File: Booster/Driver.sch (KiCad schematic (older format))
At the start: 4 parts

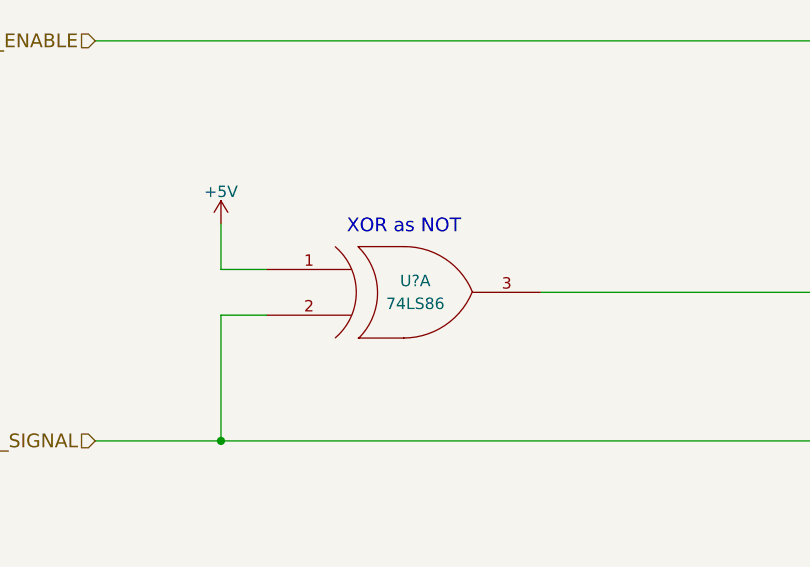
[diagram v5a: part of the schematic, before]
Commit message: Use actual test point instead of 1 pin jumpers.
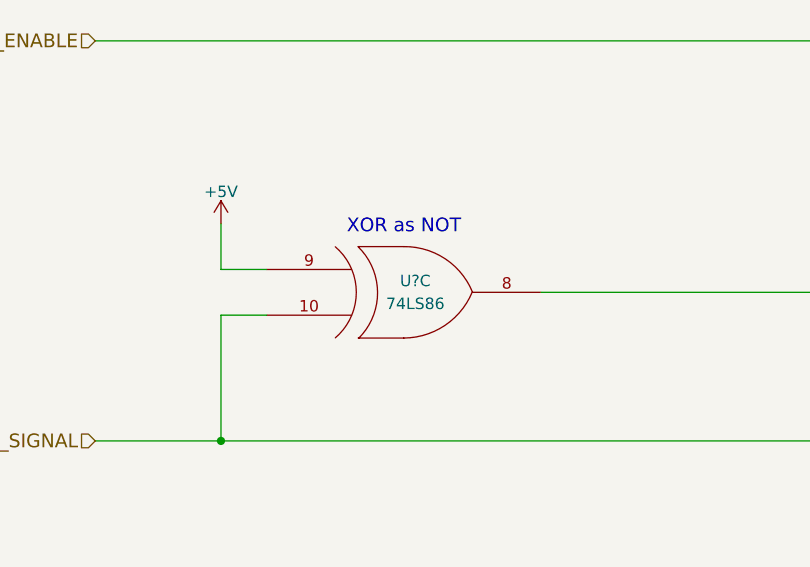
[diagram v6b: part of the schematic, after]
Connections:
- net +5V: now also U?.9 (IN1); no longer U?.1 (IN1)
- net DRIVER_SIGNAL: now also U?.10 (IN2); no longer U?.2 (IN2)
- net at IC?.15 (SIG2A), IC?.2 (SIG1A): now also U?.8 (OUT); no longer U?.3 (OUT)
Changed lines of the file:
@@
 $Comp
 L 74LS86 U?
-U 1 1 5A0F63C2
+U 3 1 5A0F63C2
 P 3800 4850
 F 0 "U?" H 3850 4900 50  0000 C CNN
@@
 F 2 "" H 3800 4850 50  0001 C CNN
 F 3 "" H 3800 4850 50  0001 C CNN
-	1    3800 4850
+	3    3800 4850
 	1    0    0    -1
 $EndComp

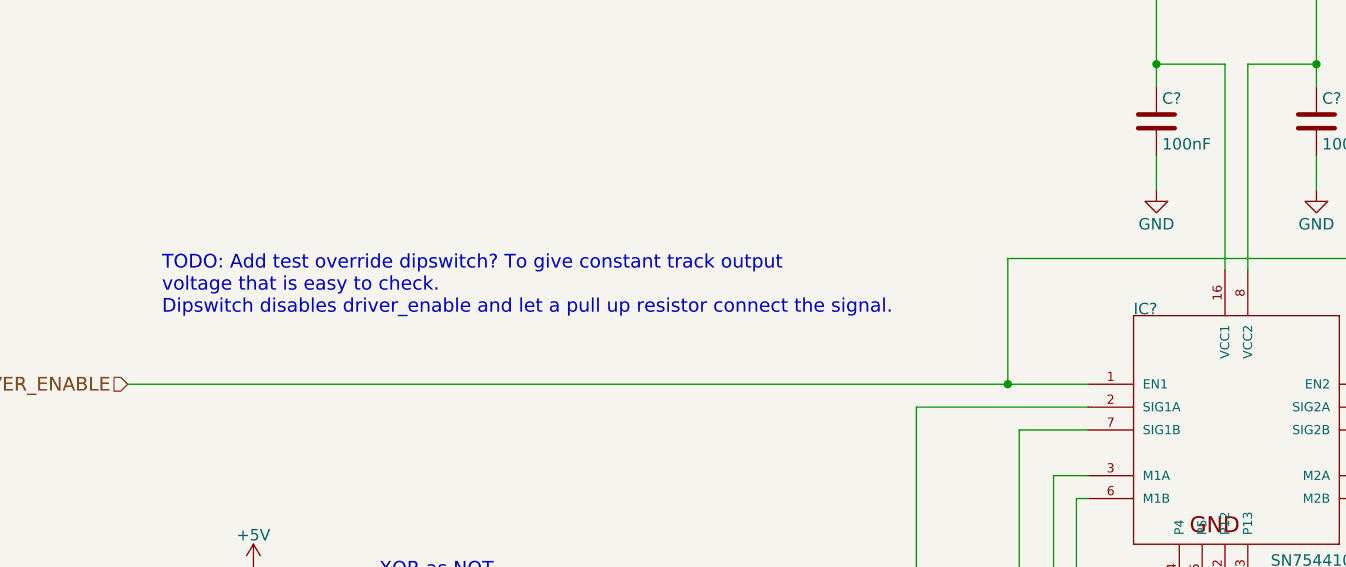
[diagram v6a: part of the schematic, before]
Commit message: Removed need for enable signal replacing it with a missing pulse detection RC based circuit.
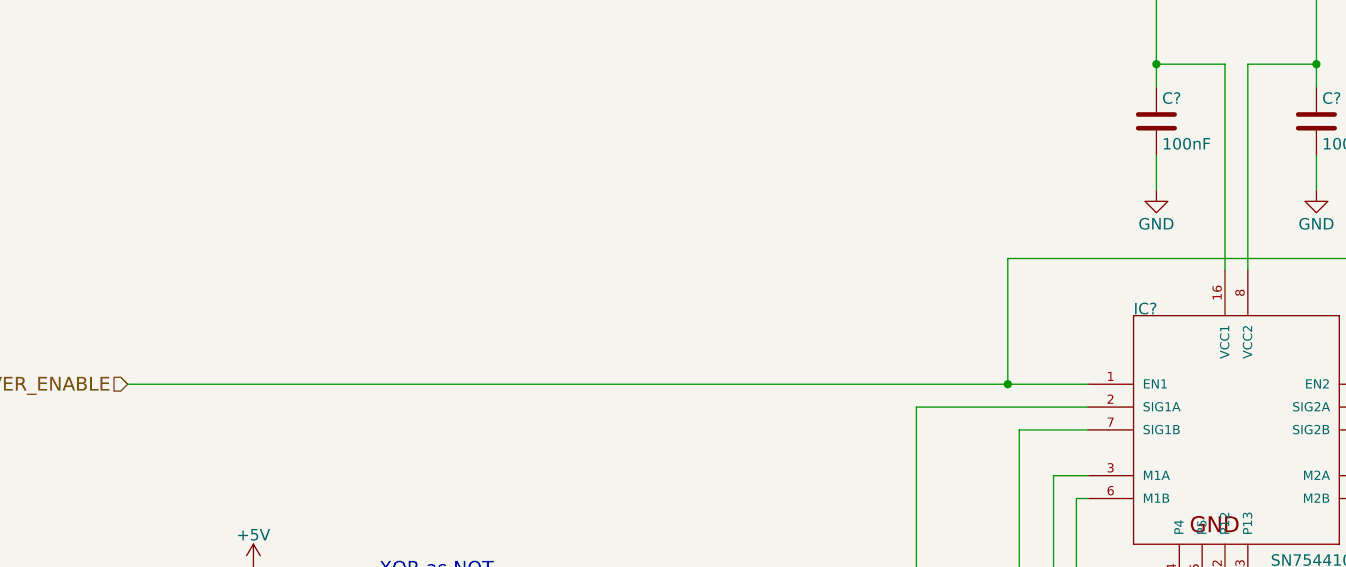
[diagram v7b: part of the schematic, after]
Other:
- note removed: "TODO: Add test override dipswitch? To give constant track output\nvoltage that is easy to check.\nDipswitch disables driver_enable and let a pull up resistor connect the signal."
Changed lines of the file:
@@
 Text Notes 3550 4600 0    60   ~ 0
 XOR as NOT
-Text Notes 2600 3450 0    60   ~ 0
-TODO: Add test override dipswitch? To give constant track output\nvoltage that is easy to check.\nDipswitch disables driver_enable and let a pull up resistor connect the signal.
 $EndSCHEMATC

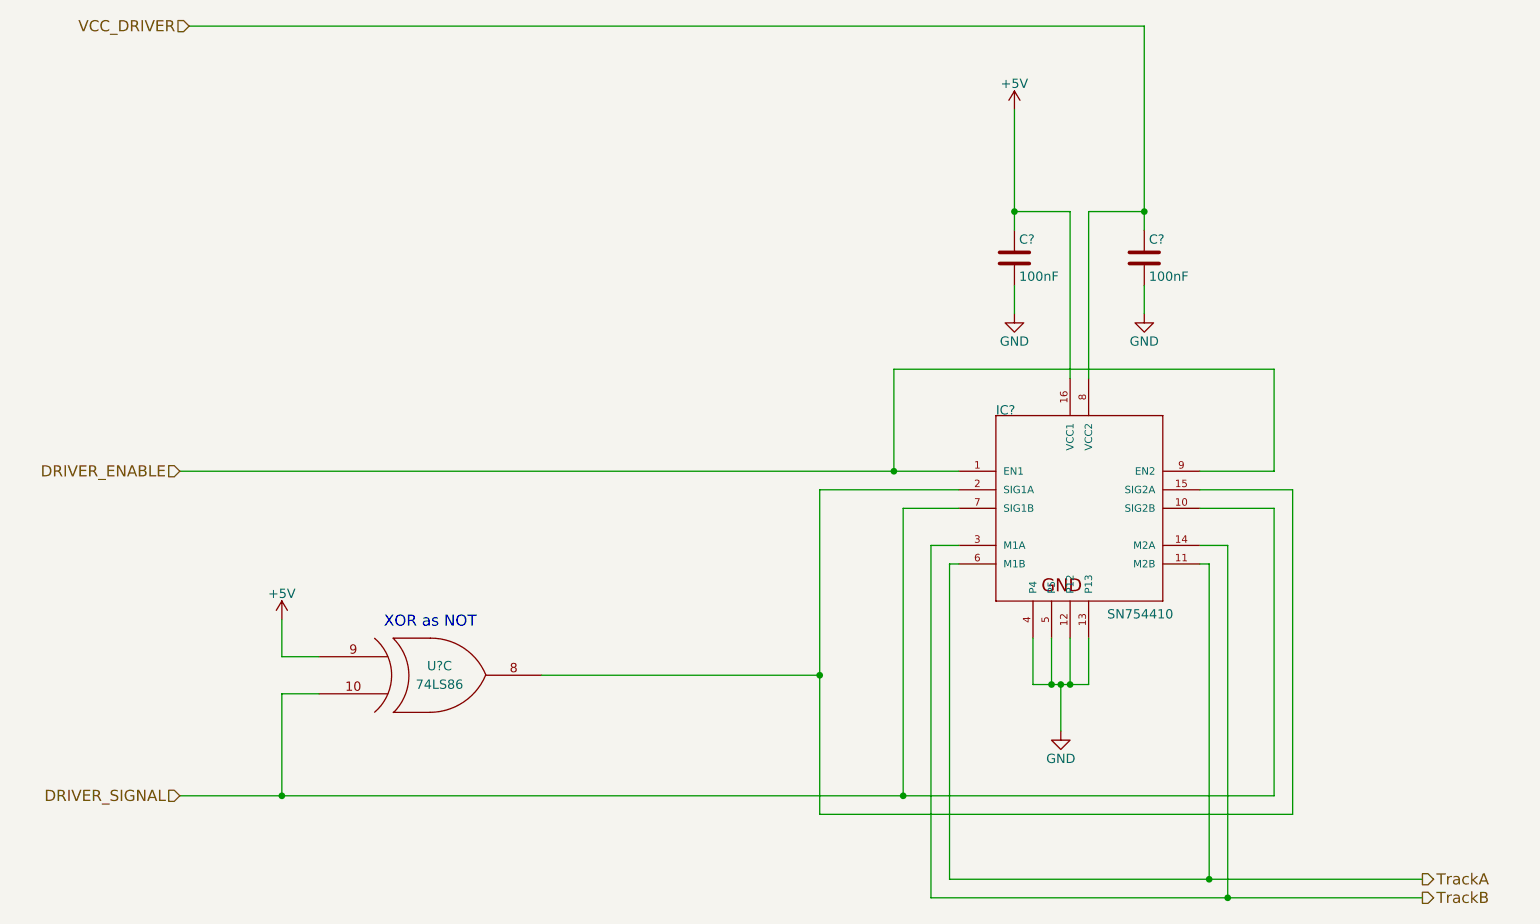
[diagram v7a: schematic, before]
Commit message: Fixed missing connections.
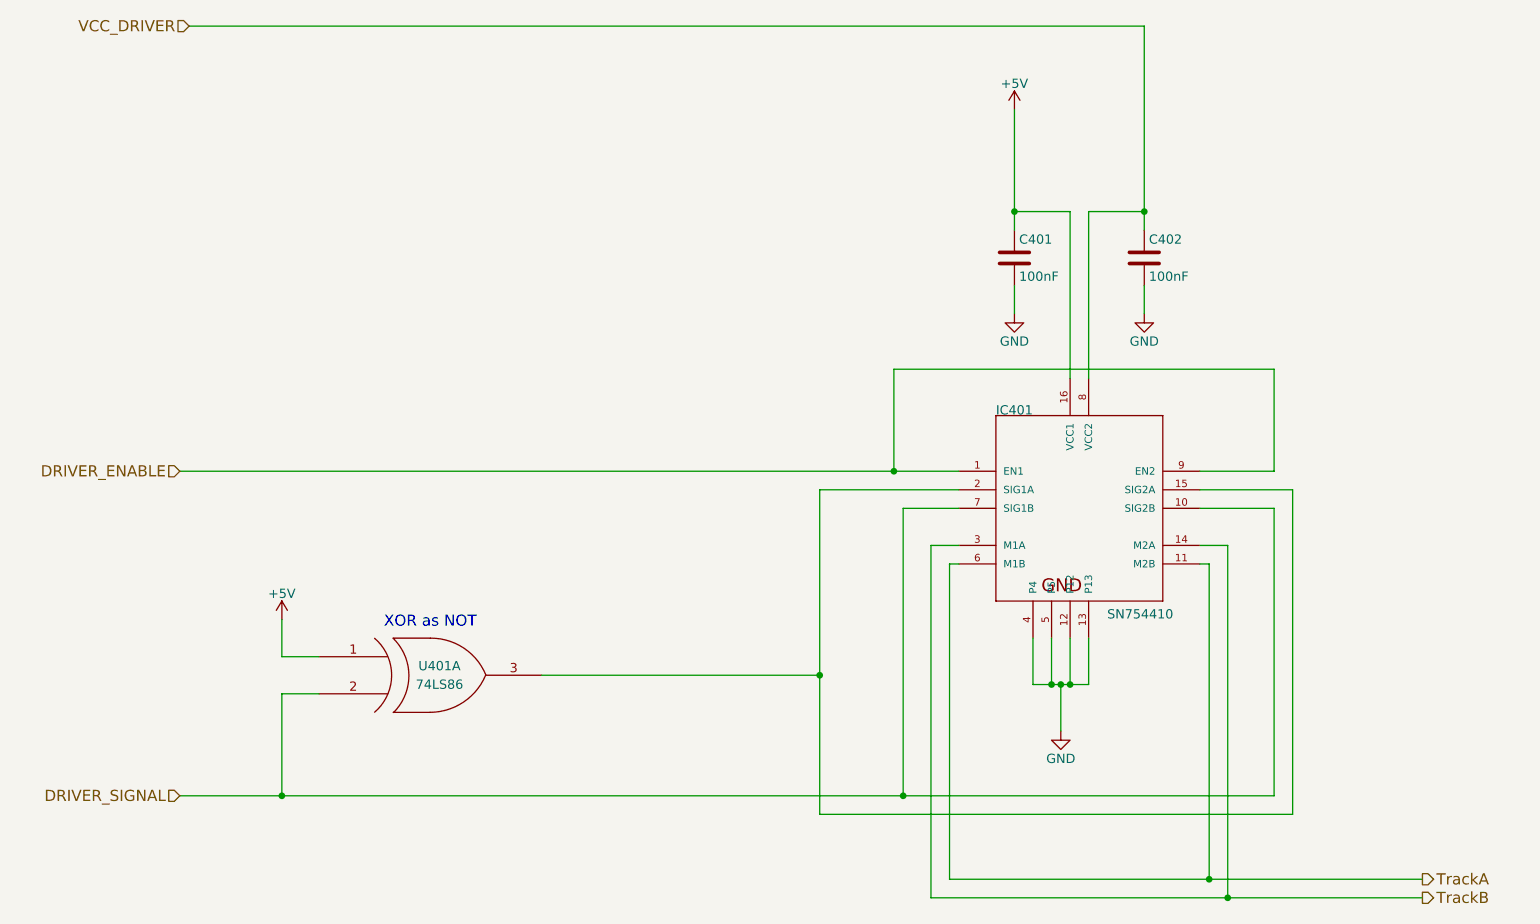
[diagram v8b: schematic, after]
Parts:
- gave numbers to parts that had none: 4
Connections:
- net +5V: now also U401.1 (IN1); no longer U401.9 (IN1)
- net DRIVER_SIGNAL: now also U401.2 (IN2); no longer U401.10 (IN2)
- net at IC401.15 (SIG2A), IC401.2 (SIG1A): now also U401.3 (OUT); no longer U401.8 (OUT)
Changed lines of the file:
@@
 P 7250 4150
 AR Path="/59E90E30" Ref="IC?"  Part="1"
-AR Path="/59E90CBD/59E90E30" Ref="IC?"  Part="1"
-F 0 "IC?" H 6850 4850 50  0000 L BNN
+AR Path="/59E90CBD/59E90E30" Ref="IC401"  Part="1"
+F 0 "IC401" H 6850 4850 50  0000 L BNN
 F 1 "SN754410" H 7450 3750 50  0000 L BNN
 F 2 "HBridge-DIP16" H 7250 4300 50  0001 C CNN
@@
 $EndComp
 $Comp
-L C C?
+L C C401
 U 1 1 59E90E3D
 P 6950 2600
-F 0 "C?" H 6975 2700 50  0000 L CNN
+F 0 "C401" H 6975 2700 50  0000 L CNN
 F 1 "100nF" H 6975 2500 50  0000 L CNN
 F 2 "" H 6988 2450 50  0001 C CNN
@@
 $EndComp
 $Comp
-L GND #PWR?
+L GND #PWR011
 U 1 1 59E90E44
 P 6950 2900
-F 0 "#PWR?" H 6950 2650 50  0001 C CNN
+F 0 "#PWR011" H 6950 2650 50  0001 C CNN
 F 1 "GND" H 6950 2750 50  0000 C CNN
 F 2 "" H 6950 2900 50  0001 C CNN
@@
 $EndComp
 $Comp
-L C C?
+L C C402
 U 1 1 59E90E4A
 P 7650 2600
-F 0 "C?" H 7675 2700 50  0000 L CNN
+F 0 "C402" H 7675 2700 50  0000 L CNN
 F 1 "100nF" H 7675 2500 50  0000 L CNN
 F 2 "" H 7688 2450 50  0001 C CNN
@@
 $EndComp
 $Comp
-L GND #PWR?
+L GND #PWR012
 U 1 1 59E90E51
 P 7650 2900
-F 0 "#PWR?" H 7650 2650 50  0001 C CNN
+F 0 "#PWR012" H 7650 2650 50  0001 C CNN
 F 1 "GND" H 7650 2750 50  0000 C CNN
 F 2 "" H 7650 2900 50  0001 C CNN
@@
 Connection ~ 7250 4900
 $Comp
-L GND #PWR?
+L GND #PWR013
 U 1 1 59E90E77
 P 7200 5150
-F 0 "#PWR?" H 7200 4900 50  0001 C CNN
+F 0 "#PWR013" H 7200 4900 50  0001 C CNN
 F 1 "GND" H 7200 5000 50  0000 C CNN
 F 2 "" H 7200 5150 50  0001 C CNN
@@
 $EndComp
 $Comp
-L +5V #PWR?
+L +5V #PWR014
 U 1 1 59E90F12
 P 6950 1800
-F 0 "#PWR?" H 6950 1650 50  0001 C CNN
+F 0 "#PWR014" H 6950 1650 50  0001 C CNN
 F 1 "+5V" H 6950 1940 50  0000 C CNN
 F 2 "" H 6950 1800 50  0001 C CNN
@@
 Connection ~ 8100 6050
 $Comp
-L 74LS86 U?
-U 3 1 5A0F63C2
+L 74LS86 U401
+U 1 1 5A0F63C2
 P 3800 4850
-F 0 "U?" H 3850 4900 50  0000 C CNN
+F 0 "U401" H 3850 4900 50  0000 C CNN
 F 1 "74LS86" H 3850 4800 50  0000 C CNN
 F 2 "" H 3800 4850 50  0001 C CNN
 F 3 "" H 3800 4850 50  0001 C CNN
-	3    3800 4850
+	1    3800 4850
 	1    0    0    -1
 $EndComp
@@
 	3000 4750 3000 4550
 $Comp
-L +5V #PWR?
+L +5V #PWR015
 U 1 1 5A0F6545
 P 3000 4550
-F 0 "#PWR?" H 3000 4400 50  0001 C CNN
+F 0 "#PWR015" H 3000 4400 50  0001 C CNN
 F 1 "+5V" H 3000 4690 50  0000 C CNN
 F 2 "" H 3000 4550 50  0001 C CNN
